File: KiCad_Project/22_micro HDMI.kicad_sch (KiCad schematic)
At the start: 20 parts, among them Q4 2SK3018, Q5 2SK3018, Q6 2SK3018, U1801 3VM11201-D730-7H

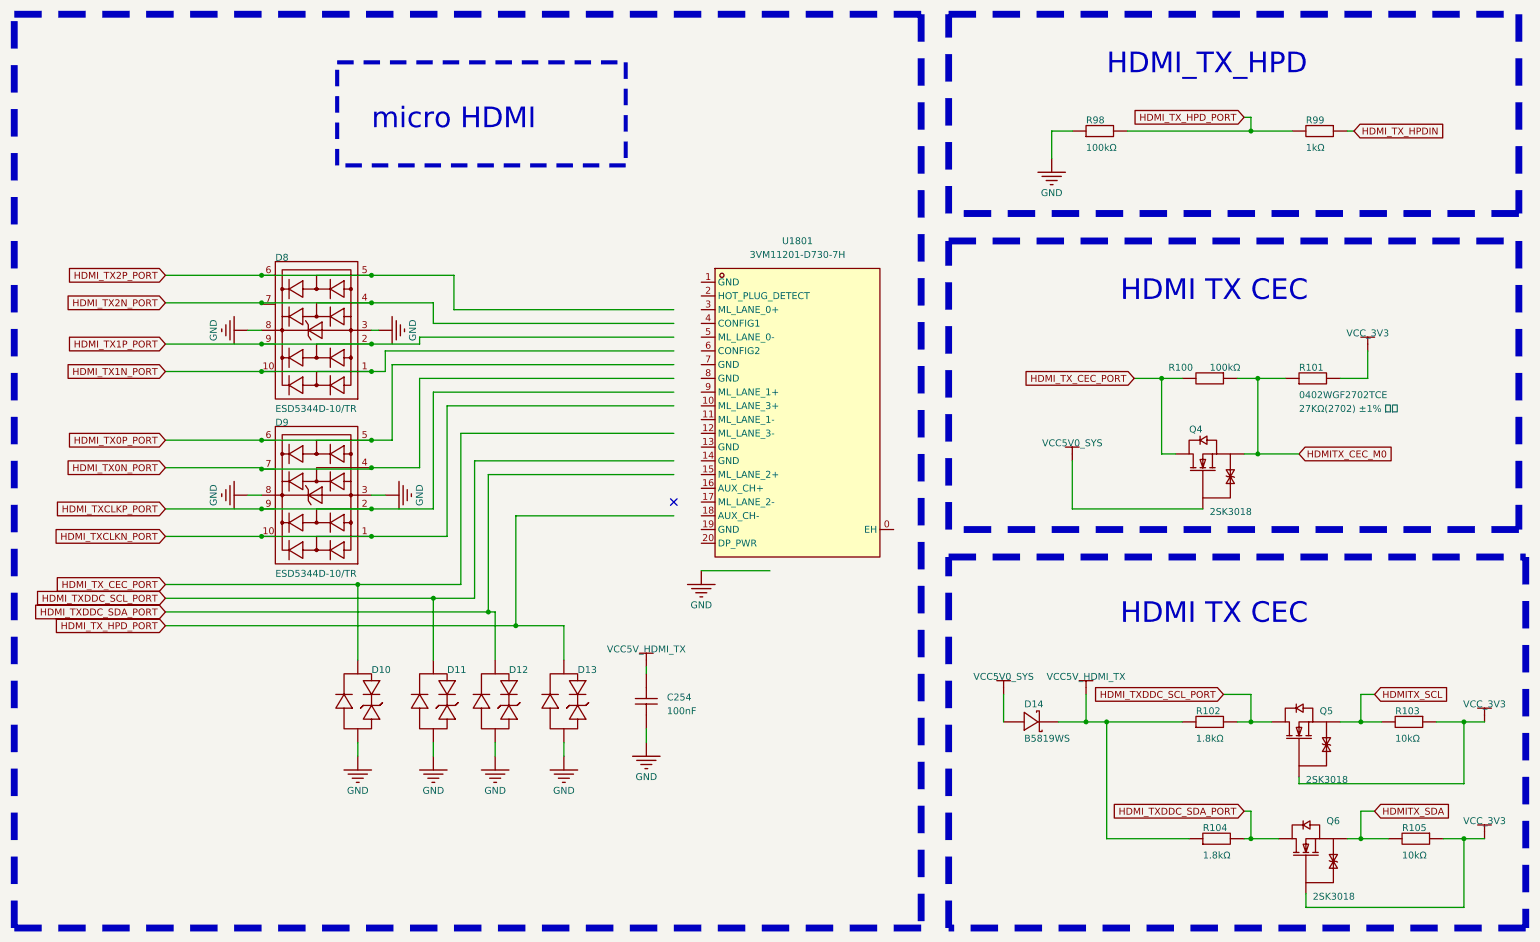
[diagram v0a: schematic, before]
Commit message: Update additional PCBs
Add WIFI PCB to get best antenna
Add Display Debbugger to get interface pinout
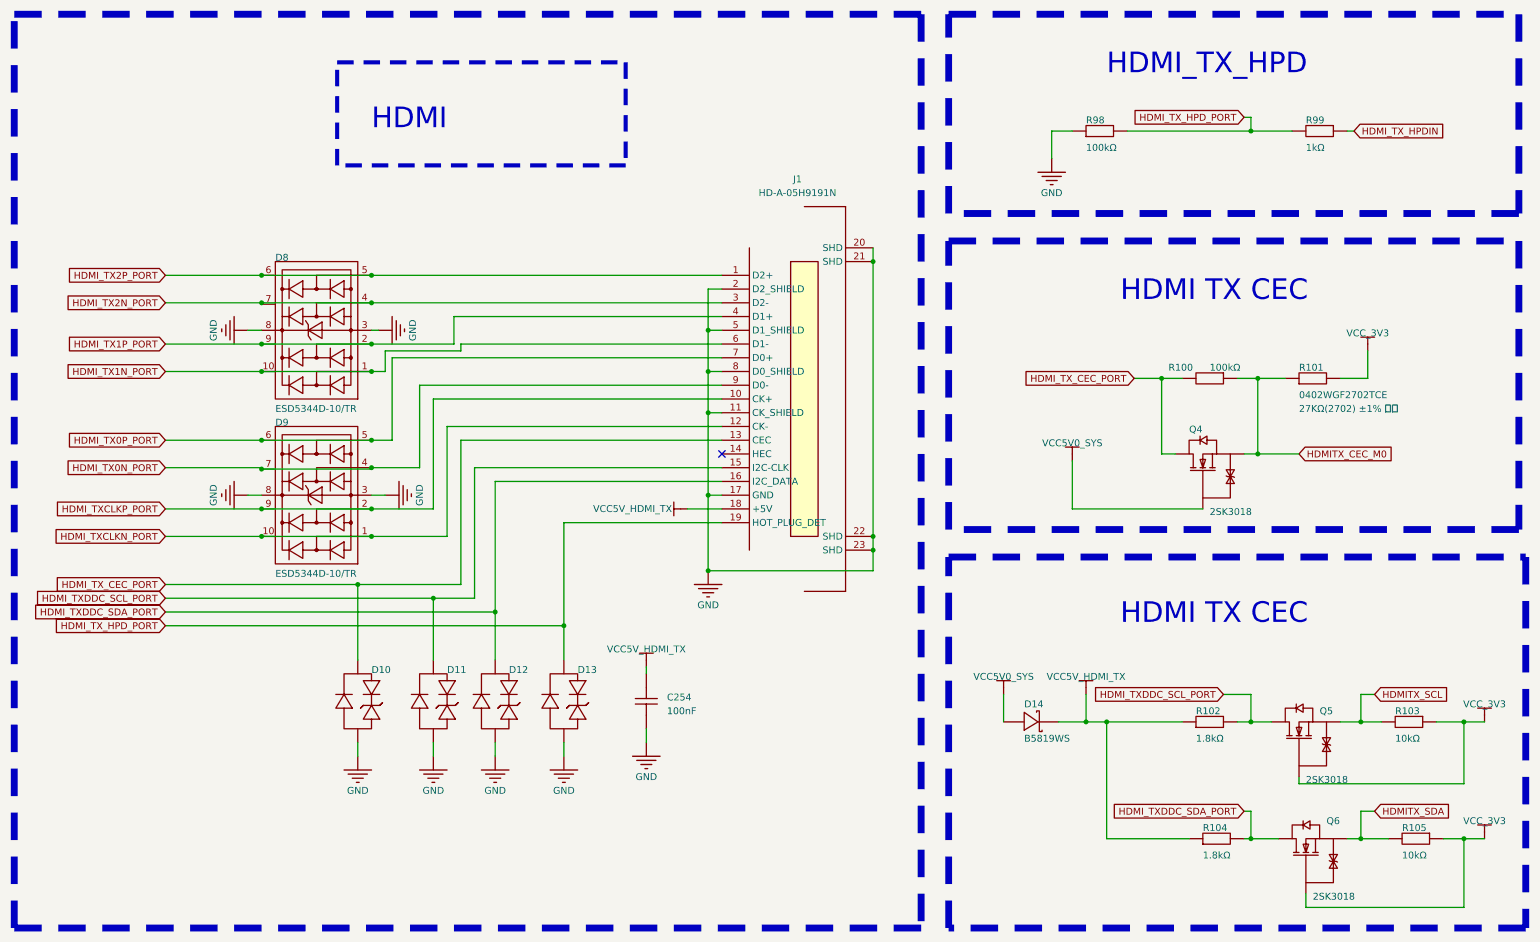
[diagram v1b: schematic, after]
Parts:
- removed U1801: 3VM11201-D730-7H, easyeda2kicad:CONN-SMD_3VM11201-D730-7H, symbol easyeda2kicad:3VM11201-D730-7H
- added J1: HD-A-05H9191N, easyeda2kicad:HDMI-SMD_HD-A-05H9192N, symbol EASYEDA2KICAD:HD-A-05H9191N
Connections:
- net GND: now also J1.11 (CK_SHIELD), J1.17 (GND), J1.2 (D2_SHIELD), J1.20 (SHD), J1.21 (SHD), J1.22 (SHD), J1.23 (SHD), J1.5 (D1_SHIELD), J1.8 (D0_SHIELD)
- net HDMI_TX0N_PORT: now also J1.9 (D0-)
- net HDMI_TX0P_PORT: now also J1.7 (D0+)
- net HDMI_TX1N_PORT: now also J1.6 (D1-)
- net HDMI_TX1P_PORT: now also J1.4 (D1+)
- net HDMI_TX2N_PORT: now also J1.3 (D2-)
- net HDMI_TX2P_PORT: now also J1.1 (D2+)
- net HDMI_TXCLKN_PORT: now also J1.12 (CK-)
- net HDMI_TXCLKP_PORT: now also J1.10 (CK+)
- net HDMI_TXDDC_SCL_PORT: now also J1.15 (I2C-CLK)
- net HDMI_TXDDC_SDA_PORT: now also J1.16 (I2C_DATA)
- net HDMI_TX_CEC_PORT: now also J1.13 (CEC)
- net HDMI_TX_HPD_PORT: now also J1.19 (HOT_PLUG_DET)
- net VCC5V_HDMI_TX: now also J1.18 (+5V)
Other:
- note added: "HDMI"
- note removed: "micro HDMI"
